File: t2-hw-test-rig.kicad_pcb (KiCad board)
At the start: 2 copper layers, 86.4 x 94 mm, 152 parts, among them J101 CONN_01X02, J102 BARREL_JACK, J103 CONN_01X02, J201 MICROUSB-TH, J202 CONN_01X02, J203 MICROUSB-TH, J204 USB_A_TH, J301 CONN_02x05, 0.05", Q101 pMOS, Q401 CJ2302, Q402 CJ2302, Q403 CJ2302, Q404 CJ2302, Q405 CJ2302 DNP, Q406 CJ2302 DNP, SW301 Switch_DPST, SW302 Switch_DPST, U101 MAX6102, U102 XC6206P332MR-G, U301 ATSAMD21J18A-MUT, U302 AAT4610, U303 AAT4610, U401 MAX9919FASA+, U402 MAX9919FASA+, U403 MAX9919FASA+, U404 MAX9919FASA+, U405 MAX9919FASA+, U501 TSV324IDT, U502 TSV324IDT, U503 TSV324IDT, X301 FC-135

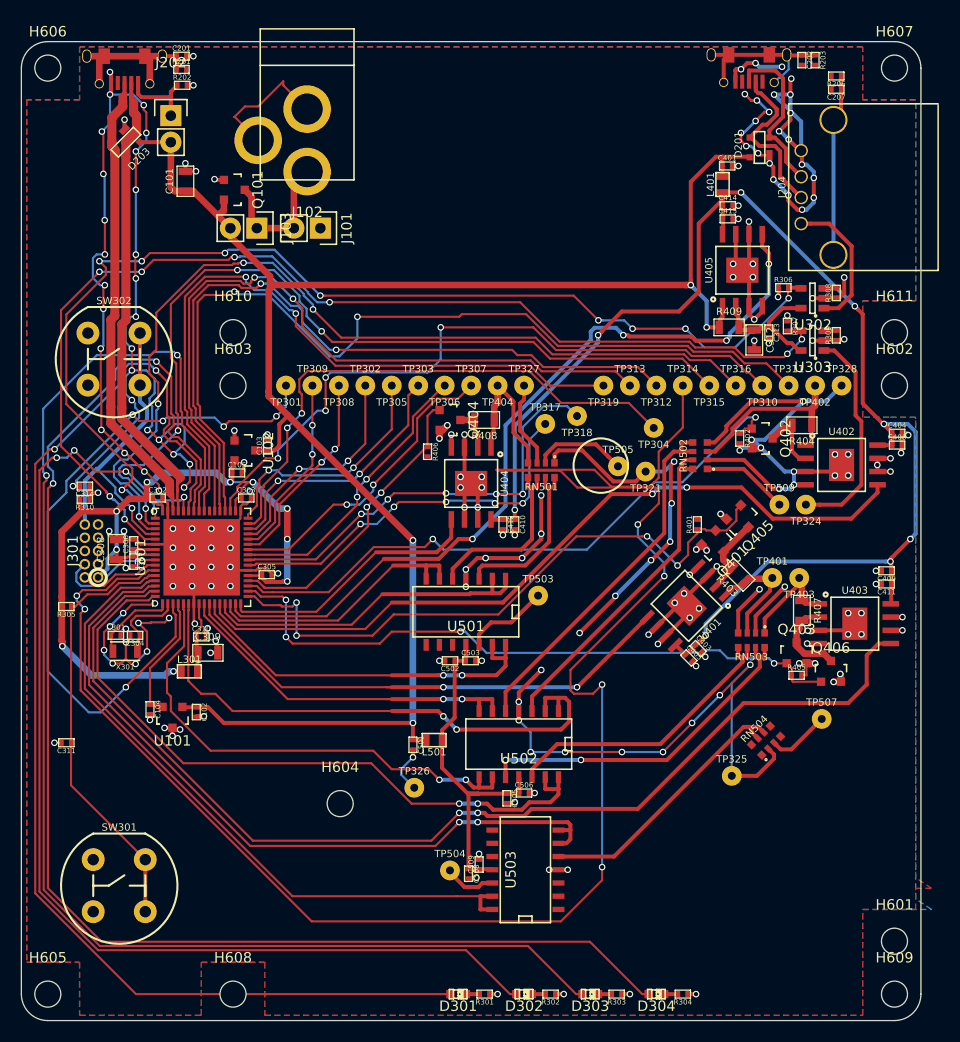
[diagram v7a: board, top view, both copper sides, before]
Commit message: passes drc except for qfn footprint...
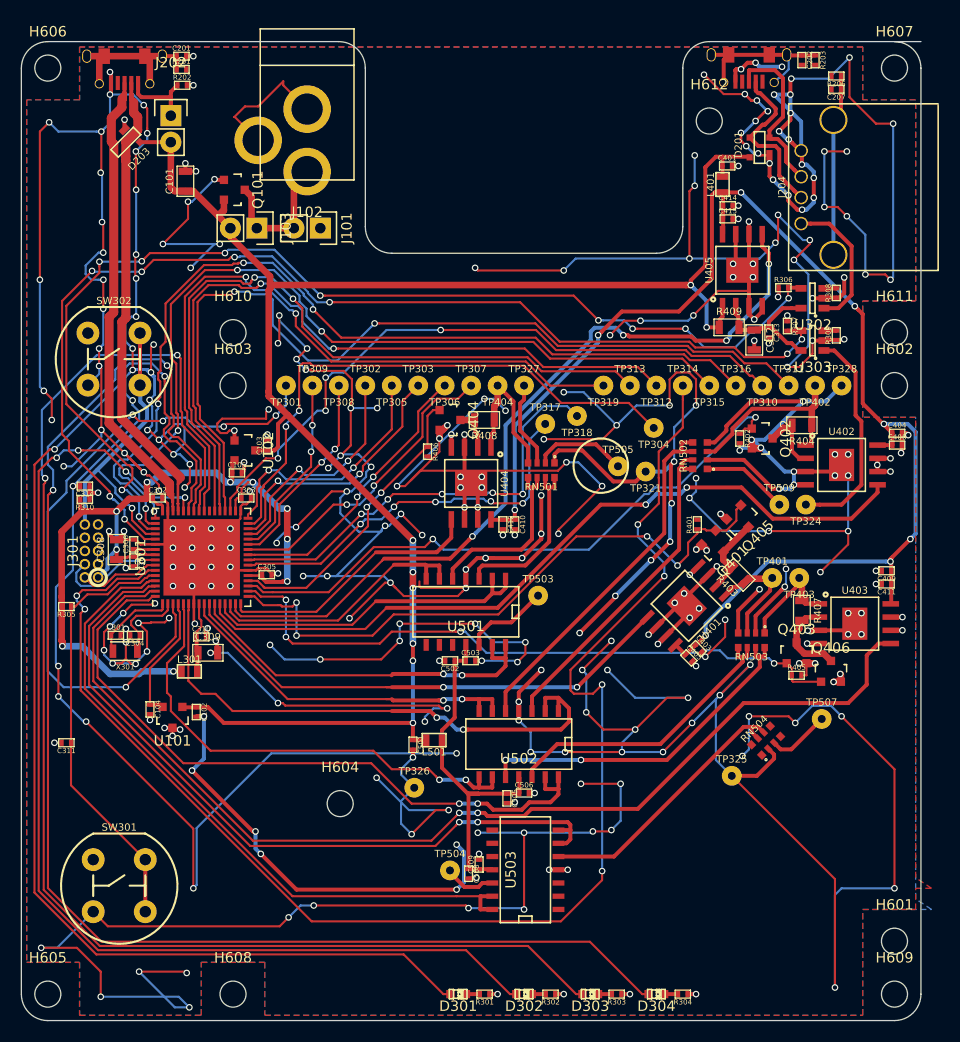
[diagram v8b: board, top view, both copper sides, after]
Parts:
- added H612: M2.5, tm-kicad-lib:MountingHole_2-5mm, F.Cu at (116.8, 66.0)
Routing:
- net GND: track 570.4 -> 1405.3 mm, vias 212 -> 336
- net /SAM/PORT_A_MOSI: track 169.0 -> 137.2 mm
- net /SAM/PORT_B_G3: track 66.5 -> 64.4 mm
- net /SAM/PORT_A_SDA: track 65.8 -> 63.8 mm
- net /SAM/UUT_~RESET: track 53.1 -> 54.2 mm
- net /SAM/PORT_A_SCK: track 88.3 -> 87.7 mm
- net /SAM/UUT_~ENABLE~_USB: track 107.4 -> 106.9 mm
- net +5V: track 177.6 -> 177.7 mm, vias 4 -> 8
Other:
- outline, holes or cut-outs redrawn
